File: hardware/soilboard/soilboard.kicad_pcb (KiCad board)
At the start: 2 copper layers, 75 parts, among them IC1 TP4056, J1 USB_C_Receptacle_USB2.0, J10 Conn_01x03, J11 Conn_01x02_Female, J12 Conn_01x06, J13 Conn_01x06, J14 Conn_01x02, J15 Conn_01x06, J16 Conn_01x06, J2 Conn_01x04, J3 Conn_01x04, J4 Conn_01x04, J5 Conn_01x03, J6 Conn_01x03, J7 Conn_01x02_Female, J8 Conn_01x03, J9 JST XH 2P 2.50mm SMD Hoz, SW1 Tactile Switch 3x4x2, SW2 Tactile Switch 3x4x2, SW3 MST22D18G2_125, T1 IRLML6344TRPBF, T2 IRLML6344TRPBF, U1 CH340K, U2 AO3401A, U3 SPX3819M5-L-3-3/TR, U4 2N27002DW, U5 ESP32-S3-WROOM-1

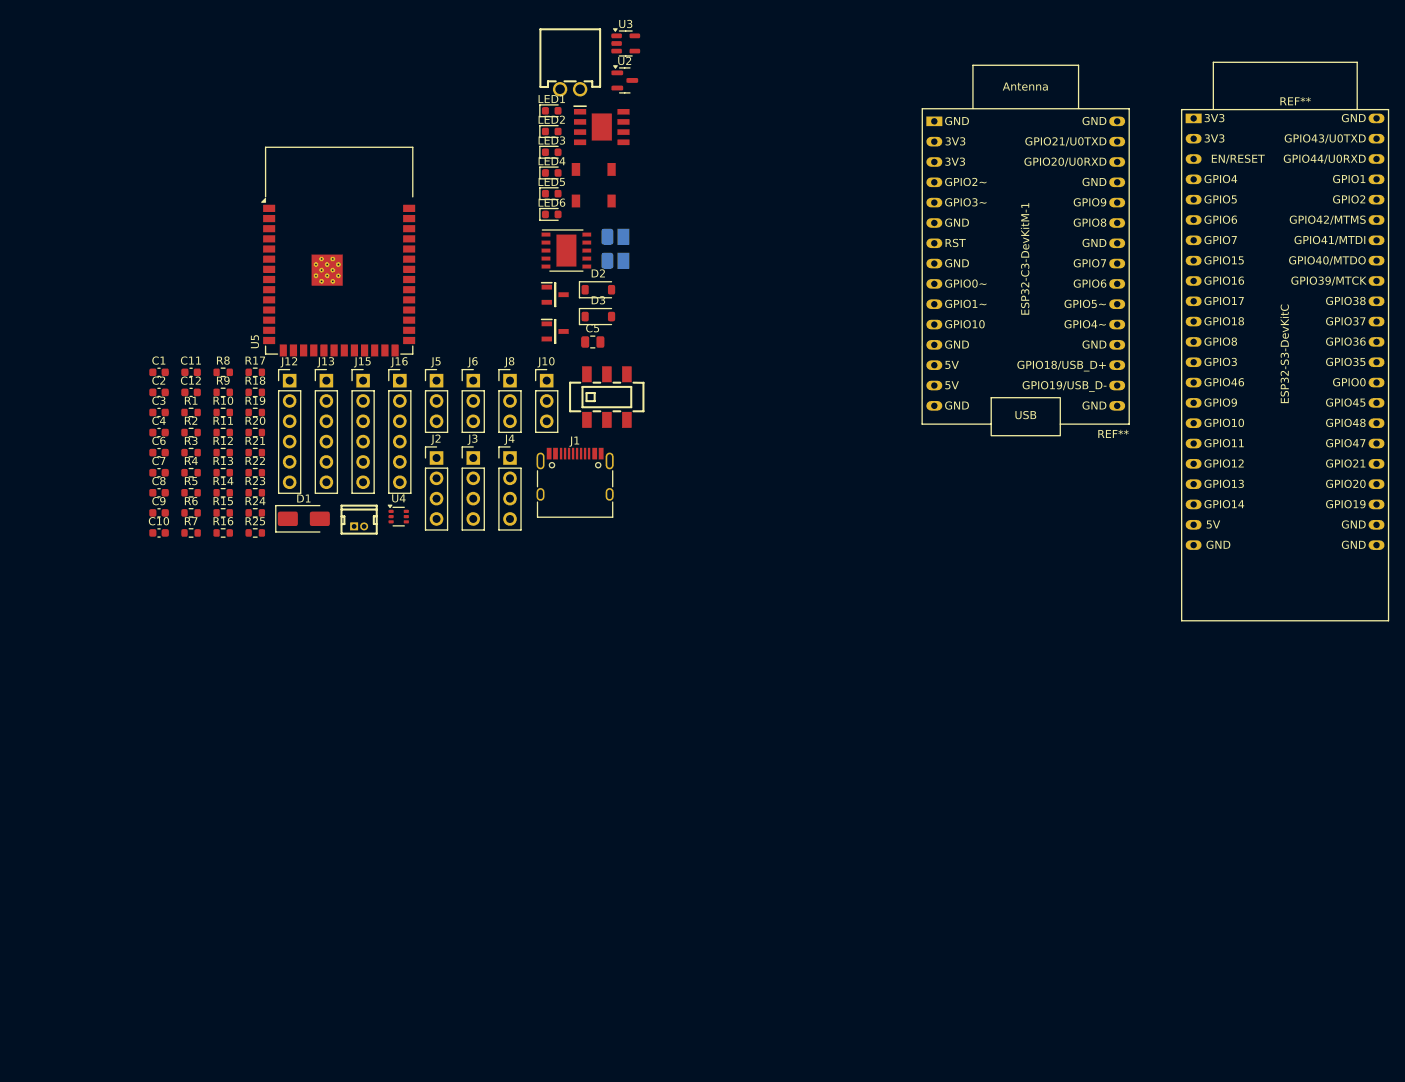
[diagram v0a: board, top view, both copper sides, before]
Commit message: Delete USB-UART interface which is no longer needed with ESP32-s3. Add eletrostatic discharge protection.
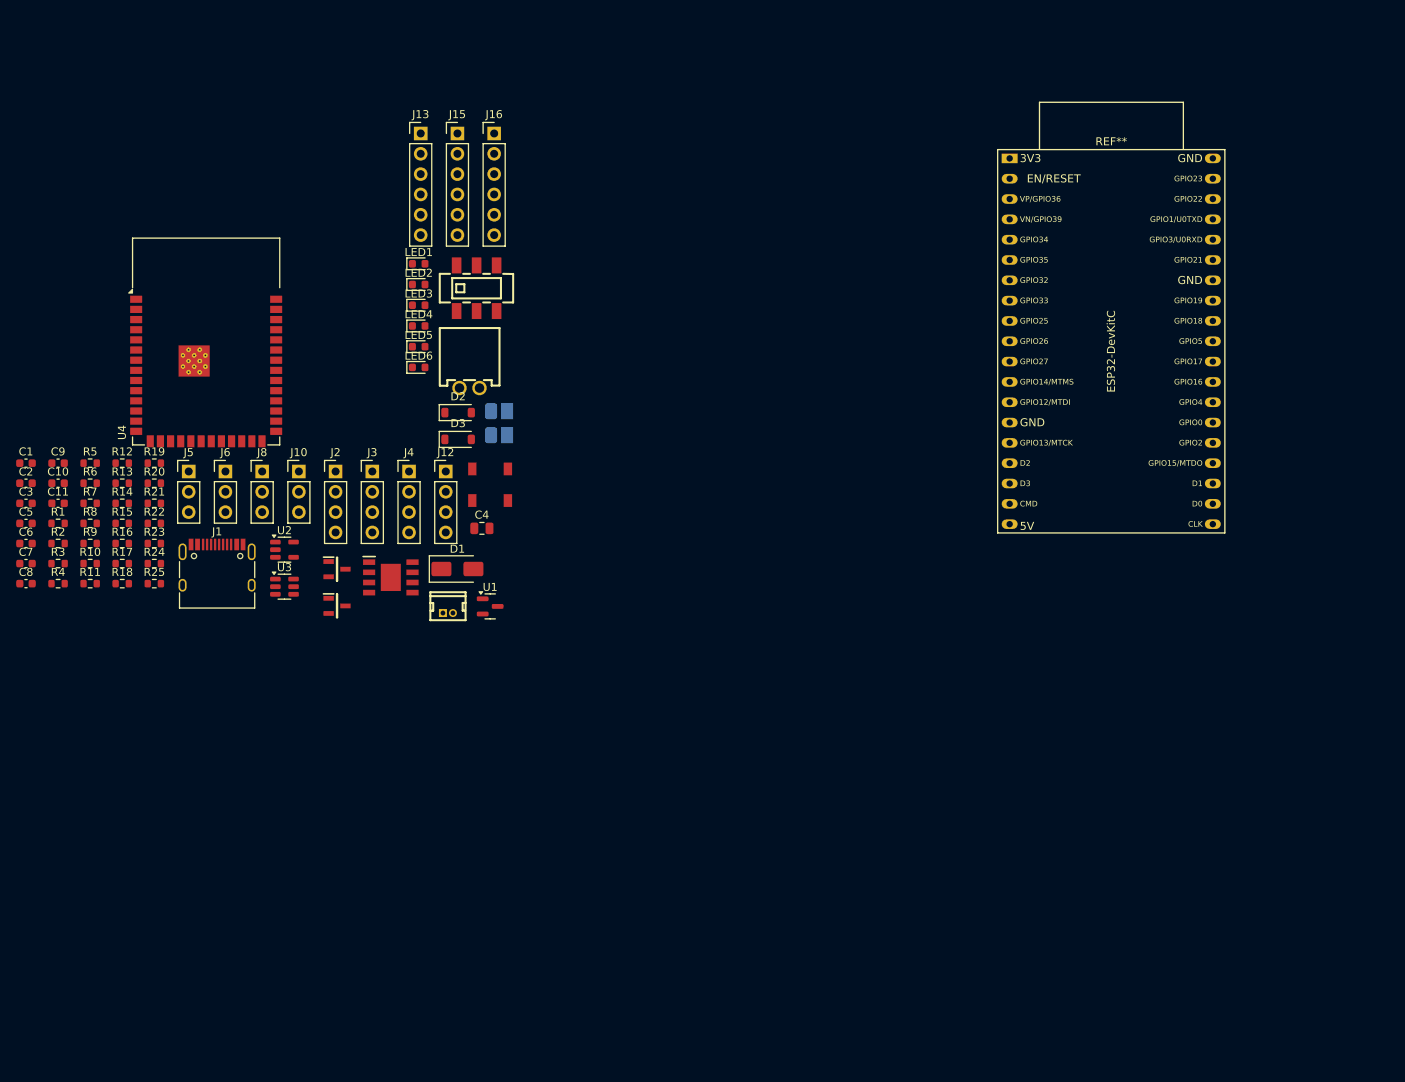
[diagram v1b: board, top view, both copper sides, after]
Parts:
- removed C12: 100nF, Capacitor_SMD:C_0603_1608Metric
- removed the REF** at (206.6, 49.4)
- removed the REF** at (239.0, 49.0)
- removed U5: ESP32-S3-WROOM-1, RF_Module:ESP32-S3-WROOM-1
- added REF**: ESP32-DevKitC, PCM_Espressif:ESP32-DevKitC, F.Cu at (216.0, 54.0)
- C1: value 100nF -> 1 uF
- C10: value 10uF -> 100nF
- C3: value 100nF -> 470pF
- C4: value 470pF -> 2.2uF; footprint Capacitor_SMD:C_0603_1608Metric -> Capacitor_SMD:C_0805_2012Metric
- C5: value 2.2uF -> 10uF; footprint Capacitor_SMD:C_0805_2012Metric -> Capacitor_SMD:C_0603_1608Metric
- C6, C8: value 10uF -> 1uF
- C7, C9: value 1uF -> 10uF
- J12: value Conn_01x06 -> Conn_01x04; footprint Connector_PinHeader_2.54mm:PinHeader_1x06_P2.54mm_Vertical -> Connector_PinHeader_2.54mm:PinHeader_1x04_P2.54mm_Vertical
- R1, R2: value 5.1K -> 1K
- R10: value 1.2K -> 1K
- R11: value 10k -> 1K
- R12: value 1K -> 10k
- R13: value 1K -> 100K
- R14, R21: value 10k -> 100K
- R15, R16, R23: value 100K -> 10k
- R4, R5: value 1K -> 5.1K
- R7: value 1K -> 470R
- R8: value 1K -> 1.2K
- R9: value 470R -> 10k
- U1: value CH340K -> AO3401A; footprint DroneV2:ESSOP-10_3.9x4.9mm_P1.00mm -> Package_TO_SOT_SMD:SOT-23
- U2: value AO3401A -> SPX3819M5-L-3-3/TR; footprint Package_TO_SOT_SMD:SOT-23 -> Package_TO_SOT_SMD:SOT-23-5
- U3: value SPX3819M5-L-3-3/TR -> USBLC6-2SC6; footprint Package_TO_SOT_SMD:SOT-23-5 -> Package_TO_SOT_SMD:SOT-23-6
- U4: value 2N27002DW -> ESP32-S3-WROOM-1; footprint Package_TO_SOT_SMD:SOT-363_SC-70-6 -> RF_Module:ESP32-S3-WROOM-1
- moved U3 80.2 mm to (125.4, 107.5)
- moved C5 74.4 mm to (93.0, 99.6)
- moved U2 72.5 mm to (125.4, 102.9)
- moved IC1 62.2 mm to (138.6, 106.4)
- moved J1 46.2 mm to (116.9, 106.3)
- moved U1 45.5 mm to (151.1, 110.0)
- moved T2 43.8 mm to (131.9, 109.9)
- moved T1 43.8 mm to (131.9, 105.3)
- moved C4 42.1 mm to (150.0, 100.2)
- moved SW2 39.6 mm to (151.1, 96.8)
- moved SW1 39.6 mm to (151.1, 92.8)
- moved J9 39.4 mm to (148.5, 82.7)
- moved J13 33.1 mm to (142.4, 50.9)
- moved J15 33.1 mm to (147.0, 50.9)
- moved J16 33.1 mm to (151.6, 50.9)
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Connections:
- C1 pad 1: GND -> VBUS
- C1 pad 2: Net-(U1-V3) -> GND
- C11 pad 1: +3V3 -> /EN
- C3 pad 1: +3V3 -> Net-(U2-BP)
- C4 pad 1: Net-(U3-BP) -> +3V3
- C6 pad 1: +3V3 -> +BATT
- C6 pad 2: GND -> Net-(D2-A)
- C7 pad 2: Net-(D2-A) -> GND
- C8 pad 2: GND -> Net-(D3-A)
- C9 pad 1: +BATT -> +3V3
- C9 pad 2: Net-(D3-A) -> GND
- J12 pad 3: /IO19 -> /IO21
- J12 pad 4: /IO20 -> /IO47
- R1 pad 1: Net-(J1-CC2) -> Net-(LED1-A)
- R1 pad 2: GND -> /LED_GREEN
- R10 pad 1: Net-(IC1-PROG) -> Net-(LED5-K)
- R10 pad 2: GND -> Net-(IC1-~{CHRG})
- R11 pad 1: GND -> Net-(LED6-K)
- R11 pad 2: /MOT_1 -> Net-(IC1-~{STDBY})
- R12 pad 1: Net-(LED5-K) -> GND
- R12 pad 2: Net-(IC1-~{CHRG}) -> /MOT_2
- R13 pad 1: Net-(LED6-K) -> +BATT
- R13 pad 2: Net-(IC1-~{STDBY}) -> /ADC_BAT
- R14 pad 1: GND -> /ADC_BAT
- R14 pad 2: /MOT_2 -> GND
- R15 pad 1: +BATT -> /SCL2
- R15 pad 2: /ADC_BAT -> +3V3
- R16 pad 1: /ADC_BAT -> /SDA2
- R16 pad 2: GND -> +3V3
- R17 pad 1: /SCL2 -> /SDA
- R18 pad 1: /SDA2 -> /SCL
- R19 pad 1: /SDA -> /EN
- R2 pad 1: Net-(J1-CC1) -> Net-(LED2-A)
- R2 pad 2: GND -> /LED_RED
- R20 pad 1: /SCL -> /IO0
- R21 pad 1: /EN -> VBUS
- R21 pad 2: +3V3 -> /LDO_H
- R22 pad 1: /IO0 -> /SDA1
- R23 pad 1: VBUS -> /SCL1
- R23 pad 2: /LDO_H -> +3V3
- R24 pad 1: /SDA1 -> GND
- R24 pad 2: +3V3 -> /RX
- R25 pad 1: /SCL1 -> GND
- R25 pad 2: +3V3 -> /TX
- R3 pad 1: Net-(LED1-A) -> Net-(LED3-A)
- R3 pad 2: /LED_GREEN -> /LED_BLUE
- R4 pad 1: Net-(LED2-A) -> Net-(J1-CC2)
- R4 pad 2: /LED_RED -> GND
- R5 pad 1: Net-(LED3-A) -> Net-(J1-CC1)
- R5 pad 2: /LED_BLUE -> GND
- R7 pad 1: /TX -> Net-(LED4-A)
- R7 pad 2: Net-(U1-RXD) -> +3V3
- R8 pad 1: /RX -> Net-(IC1-PROG)
- R8 pad 2: Net-(U1-TXD) -> GND
- R9 pad 1: Net-(LED4-A) -> GND
- R9 pad 2: +3V3 -> /MOT_1
- U1 pad 1: /D+ -> +5V
- U1 pad 2: /D- -> VBUS
- U1 pad 3: GND -> +BATT
- U2 pad 1: +5V -> VBUS
- U2 pad 2: VBUS -> GND
- U2 pad 3: +BATT -> LDO_EN
- U3 pad 1: VBUS -> /D+
- U3 pad 3: LDO_EN -> /D-
- U3 pad 4: Net-(U3-BP) -> /D_PROC-
- U3 pad 5: +3V3 -> VBUS
- U4 pad 1: /RTS -> GND
- U4 pad 2: /DTR -> +3V3
- U4 pad 3: /IO0 -> /EN
- U4 pad 4: /DTR -> /SERVO2
- U4 pad 5: /RTS -> /MOT_1
- U4 pad 6: /EN -> /MOT_2

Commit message: SOILBoard v0.3 send off for manufacturing.
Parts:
- removed J14: Conn_01x02, DroneV2:CONN-TH_1.25T-2A_1.25T-2A
- removed J15, J16: Conn_01x06, Connector_PinHeader_2.54mm:PinHeader_1x06_P2.54mm_Vertical
- removed the R15 at (105.1, 99.6)
- removed the R16 at (105.1, 102.1)
- removed R24, R25: 10k, Resistor_SMD:R_0603_1608Metric
- removed the REF** at (216.0, 54.0)
- added G***: LOGO, decals:soilguy, F.Cu at (129.0, 101.0)
- added REF**: MountingHole_2.2mm_M2, MountingHole:MountingHole_2.2mm_M2, F.Cu at (107.5, 152.0)
- added REF**: MountingHole_2.2mm_M2, MountingHole:MountingHole_2.2mm_M2, F.Cu at (163.5, 152.0)
- added REF**: MountingHole_2.2mm_M2, MountingHole:MountingHole_2.2mm_M2, F.Cu at (107.5, 74.0)
- added REF**: MountingHole_2.2mm_M2, MountingHole:MountingHole_2.2mm_M2, F.Cu at (163.4, 74.0)
- J11, J7: value Conn_01x02_Female -> Conn_01x02_Socket; footprint DroneV2:JST_PH_B2B-PH-K_1x02_P2.00mm_Vertical -> TerminalBlock:TerminalBlock_bornier-2_P5.08mm
- J12: value Conn_01x04 -> Conn_01x09_Socket; footprint Connector_PinHeader_2.54mm:PinHeader_1x04_P2.54mm_Vertical -> Connector_PinSocket_2.54mm:PinSocket_1x09_P2.54mm_Vertical
- J13: value Conn_01x06 -> Extra_01x04_Socket; footprint Connector_PinHeader_2.54mm:PinHeader_1x06_P2.54mm_Vertical -> Connector_PinHeader_2.54mm:PinHeader_1x05_P2.54mm_Vertical
- J2: value Conn_01x04 -> Temp_01x04
- J3: value Conn_01x04 -> Ping_01x04
- J4: value Conn_01x04 -> Stemma_01x04
- moved J7 80.6 mm to (114.8, 157.5), turned to -90 degrees
- moved C8 75.7 mm to (155.2, 150.4)
- moved D2 75.1 mm to (114.0, 153.2)
- moved J11 73.9 mm to (156.5, 162.3), turned to 90 degrees
- moved R12 69.6 mm to (151.4, 144.1), turned to 180 degrees
- moved C5 65.1 mm to (146.6, 136.6), turned to 90 degrees
- moved D3 64.4 mm to (156.0, 152.9)
- moved C3 62.8 mm to (138.8, 140.2)
- moved SW3 62.3 mm to (152.0, 132.5), turned to 90 degrees
- moved C7 58.7 mm to (146.9, 127.9), turned to 90 degrees
- moved LED4 58.7 mm to (142.2, 133.6), turned to -90 degrees
- moved J10 57.7 mm to (158.0, 141.9)
- moved R7 57.5 mm to (142.4, 137.1), turned to -90 degrees
- moved R5 56.8 mm to (130.0, 141.0), turned to 180 degrees
- moved C2 54.6 mm to (134.6, 130.0), turned to 90 degrees
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- renumbered R17 to R15, R18 to R16, R19 to R17, R20 to R18, R21 to R19, R22 to R20, R23 to R21
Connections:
- J12 pad 1: /IO17 -> /MISO
- J12 pad 2: /IO18 -> /LED_TFT
- J12 pad 3: /IO21 -> /SCK
- J12 pad 4: /IO47 -> /MOSI
- J13 pad 1: VBUS -> /IO15
- J13 pad 2: GND -> /IO16
- J13 pad 3: +3V3 -> /IO17
- J13 pad 4: /IO12 -> /IO18
- J13 pad 5: /SDA -> /IO8
- R12 pad 1: GND -> /MOT2
- R12 pad 2: /MOT_2 -> GND
- R15 pad 1: /SDA -> /SCL2
- R16 pad 1: /SCL -> /SDA2
- R9 pad 2: /MOT_1 -> /MOT1
- T1 pad 1: /MOT_1 -> /MOT1
- T2 pad 1: /MOT_2 -> /MOT2
- U4 pad 12: /LED_RED -> /IO8
- U4 pad 15: /SERVO1 -> /CS
- U4 pad 16: /SOIL2 -> /RESET
- U4 pad 17: /LED_GREEN -> /DC
- U4 pad 18: /SCL -> /MOSI
- U4 pad 19: /SDA -> /SCK
- U4 pad 20: /IO12 -> /LED_TFT
- U4 pad 21: /TRIG -> /SERVO1
- U4 pad 22: /ECHO -> /MISO
- U4 pad 23: /IO21 -> /SERVO2
- U4 pad 24: /IO47 -> /LED_GREEN
- U4 pad 25: /IO48 -> /LED_RED
- U4 pad 26: /SOIL1 -> /LED_BLUE
- U4 pad 28: /MOSI -> /MOT2
- U4 pad 29: /CLK -> /SOIL2
- U4 pad 30: /MISO -> /ADC_BAT
- U4 pad 31: /BUZ1 -> unconnected-(U4-IO38-Pad31)
- U4 pad 32: /BUZ2 -> unconnected-(U4-IO39-Pad32)
- U4 pad 33: /SDA1 -> unconnected-(U4-IO40-Pad33)
- U4 pad 34: /SCL1 -> /SDA2
- U4 pad 35: /CS -> /SCL2
- U4 pad 36: /RX -> unconnected-(U4-RXD0-Pad36)
- U4 pad 37: /TX -> unconnected-(U4-TXD0-Pad37)
- U4 pad 38: /ADC_BAT -> /SDA1
- U4 pad 39: /IO1 -> /SCL1
- U4 pad 4: /SERVO2 -> /ECHO
- U4 pad 5: /MOT_1 -> /TRIG
- U4 pad 6: /MOT_2 -> /SOIL1
- U4 pad 7: /LED_BLUE -> /MOT1
- U4 pad 8: /SDA2 -> /IO15
- U4 pad 9: /SCL2 -> /IO16
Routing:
- net +3V3: track 0.00 -> 234.2 mm, vias 0 -> 9
- net +BATT: track 0.00 -> 168.3 mm, vias 0 -> 4
- net GND: track 0.00 -> 99.5 mm, vias 0 -> 115
- net +5V: track 0.00 -> 72.2 mm, vias 0 -> 3
- net /MOT1: track 0.00 -> 69.9 mm
- net /SOIL1: track 0.00 -> 67.7 mm
- net /SOIL2: track 0.00 -> 64.0 mm, vias 0 -> 1
- net /D_PROC+: track 0.00 -> 63.8 mm, vias 0 -> 2
- net /MOT2: track 0.00 -> 62.5 mm, vias 0 -> 2
- net /D_PROC-: track 0.00 -> 60.8 mm, vias 0 -> 4
- net /TRIG: track 0.00 -> 55.0 mm
- net /ECHO: track 0.00 -> 53.8 mm
- net /SERVO1: track 0.00 -> 31.6 mm, vias 0 -> 1
- net /SERVO2: track 0.00 -> 27.8 mm, vias 0 -> 1
- net VBUS: track 0.00 -> 27.5 mm, vias 0 -> 3
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- added copper zone on B.Cu, net GND
- added copper zone on F.Cu, net GND
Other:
- board outline added: 61.7 x 97.3 mm
- board text added: "+3v3"
- board text added: "+BATT"
- board text added: "By L.Du"
- board text added: "ECHO/IO4"
- board text added: "GND"
- board text added: "IO15"
- board text added: "IO16"
- board text added: "IO17"
- board text added: "IO18"
- board text added: "IO8"
- board text added: "SCL1"
- board text added: "SCL2/IO42"
- board text added: "SDA1"
- board text added: "SDA2/IO41"
- board text added: "SERVO1/IO13"
- board text added: "SERVO2/IO36"
- board text added: "SOIL Board"
- board text added: "SOIL1/IO6"
- board text added: "SOIL2/IO36"
- board text added: "T1"
- board text added: "T2"
- board text added: "TRIG/IO5"
- board text added: "v0.3"
